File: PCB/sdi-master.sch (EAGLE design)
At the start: 21 parts, among them U1 ATSAMD11C14A-SSUT, U3 LDL1117S12R

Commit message: removed buttons.. not needed
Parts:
- removed R3: 2k, SparkFun-Resistors:RESISTOR1206
- removed S1: MOMENTARY-SWITCH-SPST-SMD-6.0X3.5MM, SparkFun-Switches:MOMENTARY-SWITCH-SPST-SMD-6.0X3.5MM
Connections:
- removed net N$1: R3.2, S1.1, U1.PA05/AIN3
- net 3.3V: no longer S1.2
- net GND: no longer R3.1
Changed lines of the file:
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@@
 <?xml version="1.0" encoding="utf-8"?>
 <!DOCTYPE eagle SYSTEM "eagle.dtd">
-<eagle version="9.2.2">
+<eagle version="9.3.0">
 <drawing>
 <settings>
@@
 <part name="F1" library="Adafruit" deviceset="PTCFUSE" device="-1812" value="TLC-MSMD110/24"/>
 <part name="J2" library="SparkFun-Connectors" deviceset="CONN_05" device=""/>
-<part name="S1" library="SparkFun-Switches" deviceset="MOMENTARY-SWITCH-SPST" device="-SMD-6.0X3.5MM"/>
-<part name="U$11" library="microbuilder" deviceset="3.3V" device=""/>
-<part name="U$14" library="microbuilder" deviceset="GND" device=""/>
-<part name="R3" library="SparkFun-Resistors" deviceset="RESISTOR" device="1206" value="2k"/>
 </parts>
 <sheets>
@@
 <attribute name="NAME" x="-71.12" y="53.848" size="1.778" layer="95" font="vector"/>
 </instance>
-<instance part="S1" gate="G$1" x="-68.58" y="83.82" smashed="yes">
-<attribute name="NAME" x="-68.58" y="85.344" size="1.778" layer="95" font="vector" align="bottom-center"/>
-</instance>
-<instance part="U$11" gate="G$1" x="-60.96" y="83.82" smashed="yes" rot="R270">
-<attribute name="VALUE" x="-59.944" y="85.344" size="1.27" layer="96" rot="R270"/>
-</instance>
-<instance part="U$14" gate="G$1" x="-83.82" y="81.28" smashed="yes" rot="MR0">
-<attribute name="VALUE" x="-82.296" y="78.74" size="1.27" layer="96" rot="MR0"/>
-</instance>
-<instance part="R3" gate="G$1" x="-78.74" y="83.82" smashed="yes">
-<attribute name="NAME" x="-80.01" y="85.3186" size="1.778" layer="95"/>
-<attribute name="VALUE" x="-76.2" y="84.328" size="1.778" layer="96"/>
-</instance>
 </instances>
 <busses>
@@
 <pinref part="J2" gate="G$1" pin="1"/>
 <pinref part="U$12" gate="G$1" pin="GND"/>
-</segment>
-<segment>
-<pinref part="R3" gate="G$1" pin="1"/>
-<pinref part="U$14" gate="G$1" pin="GND"/>
 </segment>
 </net>
@@
 <pinref part="J2" gate="G$1" pin="2"/>
 </segment>
-<segment>
-<pinref part="S1" gate="G$1" pin="2"/>
-<pinref part="U$11" gate="G$1" pin="3.3V"/>
-</segment>
 </net>
 <net name="SWDIO" class="0">
@@
 </segment>
 </net>
-<net name="N$1" class="0">
-<segment>
-<pinref part="S1" gate="G$1" pin="1"/>
-<pinref part="R3" gate="G$1" pin="2"/>
-<pinref part="U1" gate="G$1" pin="PA05/AIN3"/>
-<wire x1="-40.64" y1="68.58" x2="-73.66" y2="68.58" width="0.1524" layer="91"/>
-<wire x1="-73.66" y1="68.58" x2="-73.66" y2="83.82" width="0.1524" layer="91"/>
-<junction x="-73.66" y="83.82"/>
-</segment>
-</net>

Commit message: added power connectors to sdi master
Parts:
- added J3: 1X2-3.5MM, Adafruit:1X2-3.5MM
- added J4: POWER_JACKPTH_LOCK, SparkFun-Connectors:POWER_JACKPTH_LOCK
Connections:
- net GND: now also J3.2, J4.GND, J4.GNDBREAK
- net VCC-RAW: now also J3.1, J4.PWR
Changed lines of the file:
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@@
 <?xml version="1.0" encoding="utf-8"?>
 <!DOCTYPE eagle SYSTEM "eagle.dtd">
-<eagle version="9.3.0">
+<eagle version="9.2.2">
 <drawing>
 <settings>
@@
 <part name="F1" library="Adafruit" deviceset="PTCFUSE" device="-1812" value="TLC-MSMD110/24"/>
 <part name="J2" library="SparkFun-Connectors" deviceset="CONN_05" device=""/>
+<part name="J3" library="Adafruit" deviceset="1X2" device="-3.5MM"/>
+<part name="GND1" library="supply1" library_urn="urn:adsk.eagle:library:371" deviceset="GND" device=""/>
+<part name="J4" library="SparkFun-Connectors" deviceset="POWER_JACK" device="PTH_LOCK"/>
+<part name="GND2" library="supply1" library_urn="urn:adsk.eagle:library:371" deviceset="GND" device=""/>
 </parts>
 <sheets>
@@
 <attribute name="NAME" x="-71.12" y="53.848" size="1.778" layer="95" font="vector"/>
 </instance>
+<instance part="J3" gate="G$1" x="22.86" y="10.16" smashed="yes"/>
+<instance part="GND1" gate="1" x="17.78" y="7.62" smashed="yes" rot="MR0">
+<attribute name="VALUE" x="20.32" y="5.08" size="1.778" layer="96" rot="MR0"/>
+</instance>
+<instance part="J4" gate="G$1" x="20.32" y="-12.7" smashed="yes" rot="MR0">
+<attribute name="VALUE" x="30.48" y="-2.54" size="1.778" layer="96" font="vector" rot="MR0"/>
+<attribute name="NAME" x="30.48" y="-12.7" size="1.778" layer="95" font="vector" rot="MR0"/>
+</instance>
+<instance part="GND2" gate="1" x="17.78" y="-12.7" smashed="yes" rot="MR0">
+<attribute name="VALUE" x="20.32" y="-15.24" size="1.778" layer="96" rot="MR0"/>
+</instance>
 </instances>
 <busses>
@@
 <pinref part="U$12" gate="G$1" pin="GND"/>
 </segment>
+<segment>
+<pinref part="J4" gate="G$1" pin="GND"/>
+<pinref part="GND2" gate="1" pin="GND"/>
+<pinref part="J4" gate="G$1" pin="GNDBREAK"/>
+<wire x1="17.78" y1="-10.16" x2="17.78" y2="-7.62" width="0.1524" layer="91"/>
+<junction x="17.78" y="-10.16"/>
+</segment>
+<segment>
+<pinref part="J3" gate="G$1" pin="2"/>
+<pinref part="GND1" gate="1" pin="GND"/>
+</segment>
 </net>
 <net name="PWM" class="0">
@@
 <pinref part="VCC-CLIP3" gate="CLIP" pin="INPUT"/>
 </segment>
+<segment>
+<label x="7.62" y="12.7" size="1.778" layer="95"/>
+<pinref part="J3" gate="G$1" pin="1"/>
+<wire x1="7.62" y1="12.7" x2="17.78" y2="12.7" width="0.1524" layer="91"/>
+</segment>
+<segment>
+<pinref part="J4" gate="G$1" pin="PWR"/>
+<wire x1="17.78" y1="-5.08" x2="7.62" y2="-5.08" width="0.1524" layer="91"/>
+<label x="5.08" y="-5.08" size="1.778" layer="95"/>
+</segment>
 </net>

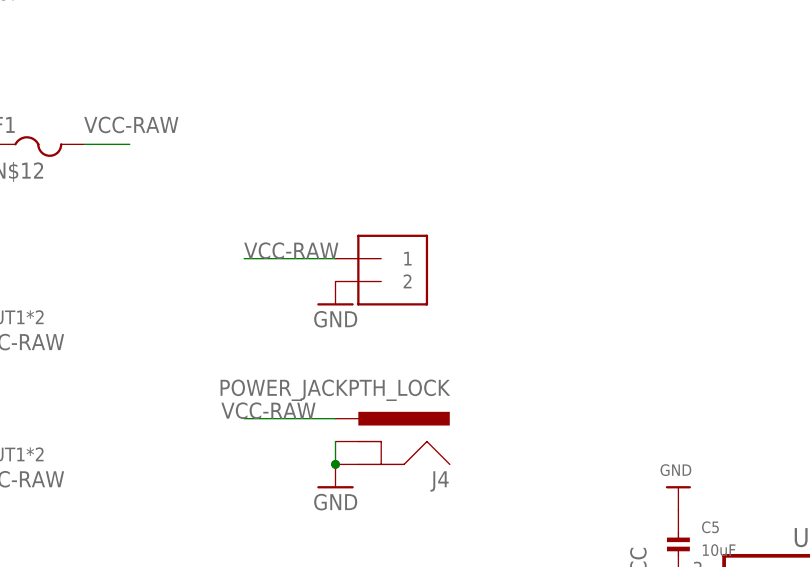
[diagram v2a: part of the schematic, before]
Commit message: replaced 2 position terminal with 3 positions
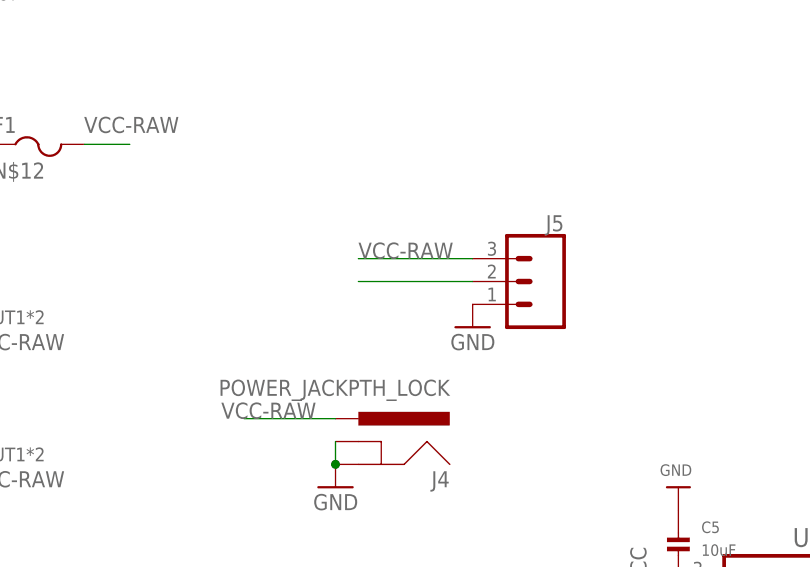
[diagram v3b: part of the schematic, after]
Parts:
- removed J3: 1X2-3.5MM, Adafruit:1X2-3.5MM
- added J5: (no value), SparkFun-Connectors:CONN_03SCREW-NS
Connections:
- net BUS: now also J5.2
- net GND: now also J5.1; no longer J3.2
- net VCC-RAW: now also J5.3; no longer J3.1
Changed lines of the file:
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@@
 <?xml version="1.0" encoding="utf-8"?>
 <!DOCTYPE eagle SYSTEM "eagle.dtd">
-<eagle version="9.2.2">
+<eagle version="9.3.0">
 <drawing>
 <settings>
@@
 <part name="F1" library="Adafruit" deviceset="PTCFUSE" device="-1812" value="TLC-MSMD110/24"/>
 <part name="J2" library="SparkFun-Connectors" deviceset="CONN_05" device=""/>
-<part name="J3" library="Adafruit" deviceset="1X2" device="-3.5MM"/>
 <part name="GND1" library="supply1" library_urn="urn:adsk.eagle:library:371" deviceset="GND" device=""/>
 <part name="J4" library="SparkFun-Connectors" deviceset="POWER_JACK" device="PTH_LOCK"/>
 <part name="GND2" library="supply1" library_urn="urn:adsk.eagle:library:371" deviceset="GND" device=""/>
+<part name="J5" library="SparkFun-Connectors" library_urn="urn:adsk.eagle:library:513" deviceset="CONN_03" device="SCREW-NS" package3d_urn="urn:adsk.eagle:package:38088/1"/>
 </parts>
 <sheets>
@@
 <attribute name="NAME" x="-71.12" y="53.848" size="1.778" layer="95" font="vector"/>
 </instance>
-<instance part="J3" gate="G$1" x="22.86" y="10.16" smashed="yes"/>
-<instance part="GND1" gate="1" x="17.78" y="7.62" smashed="yes" rot="MR0">
-<attribute name="VALUE" x="20.32" y="5.08" size="1.778" layer="96" rot="MR0"/>
+<instance part="GND1" gate="1" x="33.02" y="5.08" smashed="yes" rot="MR0">
+<attribute name="VALUE" x="35.56" y="2.54" size="1.778" layer="96" rot="MR0"/>
 </instance>
 <instance part="J4" gate="G$1" x="20.32" y="-12.7" smashed="yes" rot="MR0">
@@
 <instance part="GND2" gate="1" x="17.78" y="-12.7" smashed="yes" rot="MR0">
 <attribute name="VALUE" x="20.32" y="-15.24" size="1.778" layer="96" rot="MR0"/>
+</instance>
+<instance part="J5" gate="J$1" x="40.64" y="10.16" smashed="yes" rot="MR0">
+<attribute name="VALUE" x="43.18" y="2.794" size="1.778" layer="96" font="vector" rot="MR0"/>
+<attribute name="NAME" x="43.18" y="15.748" size="1.778" layer="95" font="vector" rot="MR0"/>
 </instance>
 </instances>
@@
 </segment>
 <segment>
-<pinref part="J3" gate="G$1" pin="2"/>
+<pinref part="J5" gate="J$1" pin="1"/>
 <pinref part="GND1" gate="1" pin="GND"/>
 </segment>
@@
 </segment>
 <segment>
-<label x="7.62" y="12.7" size="1.778" layer="95"/>
-<pinref part="J3" gate="G$1" pin="1"/>
-<wire x1="7.62" y1="12.7" x2="17.78" y2="12.7" width="0.1524" layer="91"/>
+<label x="20.32" y="12.7" size="1.778" layer="95"/>
+<wire x1="20.32" y1="12.7" x2="33.02" y2="12.7" width="0.1524" layer="91"/>
+<pinref part="J5" gate="J$1" pin="3"/>
 </segment>
 <segment>
@@
 <label x="-55.88" y="58.42" size="1.778" layer="95"/>
 </segment>
-</net>
+<segment>
+<pinref part="J5" gate="J$1" pin="2"/>
+<wire x1="33.02" y1="10.16" x2="20.32" y2="10.16" width="0.1524" layer="91"/>
+</segment>
+</net>
